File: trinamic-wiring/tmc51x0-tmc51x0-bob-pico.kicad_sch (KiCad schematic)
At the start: 4 parts, among them M1 Stepper_Motor

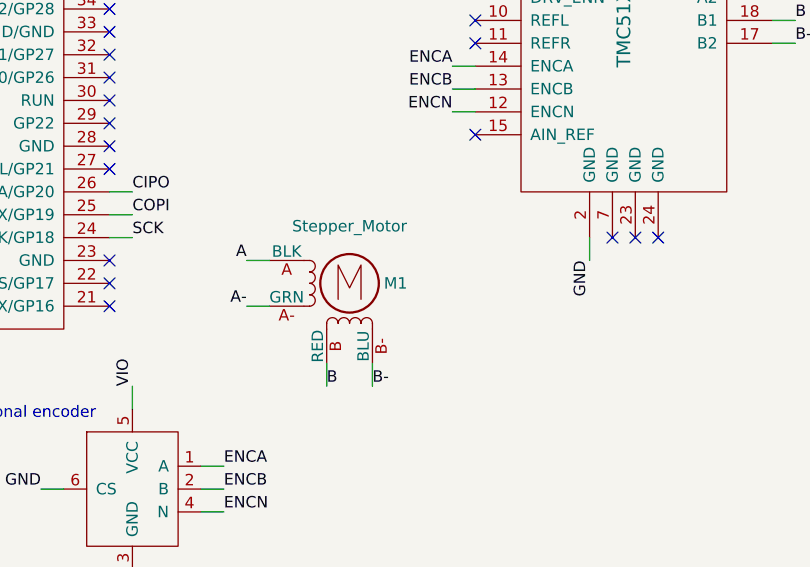
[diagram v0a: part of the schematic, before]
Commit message: Split tmc51x0 into spi and uart
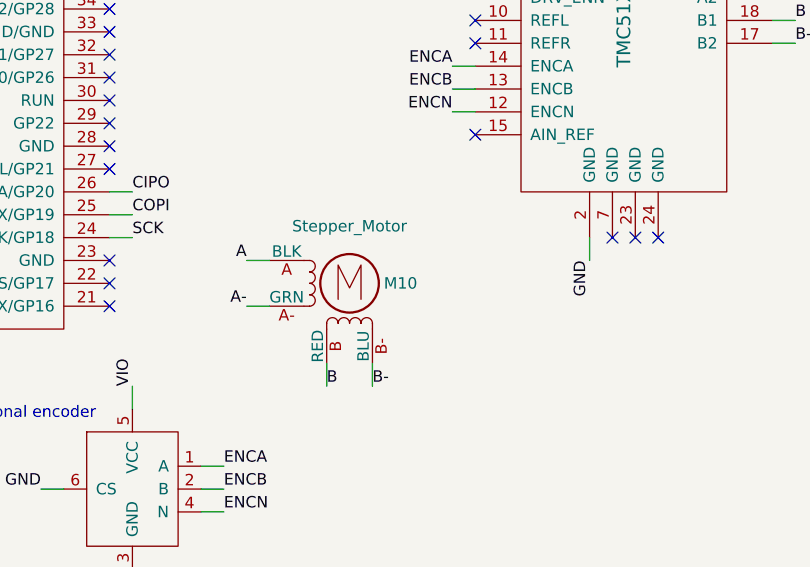
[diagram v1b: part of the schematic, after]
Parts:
- renumbered A3 to A5, BOB1 to BOB2, ENC1 to ENC2, M1 to M10
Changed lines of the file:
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@@
   (title_block
     (title "Trinamic Wiring")
-    (date "2024-07-31")
+    (date "2024-08-01")
     (rev "0.5")
     (company "Janelia Research Campus")
@@
   (symbol (lib_id "Janelia:Stepper_Motor_QSH2818-32-07-006") (at 149.86 133.35 0) (unit 1)
     (in_bom yes) (on_board yes) (dnp no)
-    (property "Reference" "M1" (at 153.67 133.35 0)
+    (property "Reference" "M10" (at 153.67 133.35 0)
       (effects (font (size 1.27 1.27)) (justify left))
     )
@@
     (instances
       (project "trinamic-wiring"
-        (path "/e4144788-6304-493f-818e-5d881d3b7418/a161638e-a96f-4455-865a-1d7502675f43/176cb0b5-cab1-47ac-9998-e59b71e39393/dab15df5-b51f-4c1f-8fc9-49b45f8778bf"
-          (reference "M1") (unit 1)
+        (path "/e4144788-6304-493f-818e-5d881d3b7418/a161638e-a96f-4455-865a-1d7502675f43/ca35872a-a0db-401c-97bd-5b4a3f731cf1/abe2ac4d-e9f3-44e3-a772-2451bb376256/dab15df5-b51f-4c1f-8fc9-49b45f8778bf"
+          (reference "M10") (unit 1)
         )
       )
@@
   (symbol (lib_id "Janelia:PICO_HEADERS") (at 80.01 111.76 0) (unit 1)
     (in_bom yes) (on_board yes) (dnp no) (fields_autoplaced)
-    (property "Reference" "A3" (at 115.57 82.55 0) (do_not_autoplace)
+    (property "Reference" "A5" (at 115.57 82.55 0) (do_not_autoplace)
       (effects (font (size 1.524 1.524)) hide)
     )
@@
     (instances
       (project "trinamic-wiring"
-        (path "/e4144788-6304-493f-818e-5d881d3b7418/a161638e-a96f-4455-865a-1d7502675f43/176cb0b5-cab1-47ac-9998-e59b71e39393/dab15df5-b51f-4c1f-8fc9-49b45f8778bf"
-          (reference "A3") (unit 1)
+        (path "/e4144788-6304-493f-818e-5d881d3b7418/a161638e-a96f-4455-865a-1d7502675f43/ca35872a-a0db-401c-97bd-5b4a3f731cf1/abe2ac4d-e9f3-44e3-a772-2451bb376256/dab15df5-b51f-4c1f-8fc9-49b45f8778bf"
+          (reference "A5") (unit 1)
         )
       )
@@
   (symbol (lib_id "Janelia:ENCODER_EMS22Q") (at 125.73 156.21 0) (unit 1)
     (in_bom yes) (on_board yes) (dnp no) (fields_autoplaced)
-    (property "Reference" "ENC1" (at 128.27 148.59 0)
+    (property "Reference" "ENC2" (at 128.27 148.59 0)
       (effects (font (size 1.524 1.524)) hide)
     )
@@
     (instances
       (project "trinamic-wiring"
-        (path "/e4144788-6304-493f-818e-5d881d3b7418/a161638e-a96f-4455-865a-1d7502675f43/176cb0b5-cab1-47ac-9998-e59b71e39393/dab15df5-b51f-4c1f-8fc9-49b45f8778bf"
-          (reference "ENC1") (unit 1)
+        (path "/e4144788-6304-493f-818e-5d881d3b7418/a161638e-a96f-4455-865a-1d7502675f43/ca35872a-a0db-401c-97bd-5b4a3f731cf1/abe2ac4d-e9f3-44e3-a772-2451bb376256/dab15df5-b51f-4c1f-8fc9-49b45f8778bf"
+          (reference "ENC2") (unit 1)
         )
       )
@@
   (symbol (lib_id "Janelia:TMC51X0_BOB") (at 180.34 102.87 0) (unit 1)
     (in_bom yes) (on_board yes) (dnp no)
-    (property "Reference" "BOB1" (at 180.34 129.54 0)
+    (property "Reference" "BOB2" (at 180.34 129.54 0)
       (effects (font (size 1.524 1.524)) hide)
     )
@@
     (instances
       (project "trinamic-wiring"
-        (path "/e4144788-6304-493f-818e-5d881d3b7418/a161638e-a96f-4455-865a-1d7502675f43/176cb0b5-cab1-47ac-9998-e59b71e39393/dab15df5-b51f-4c1f-8fc9-49b45f8778bf"
-          (reference "BOB1") (unit 1)
+        (path "/e4144788-6304-493f-818e-5d881d3b7418/a161638e-a96f-4455-865a-1d7502675f43/ca35872a-a0db-401c-97bd-5b4a3f731cf1/abe2ac4d-e9f3-44e3-a772-2451bb376256/dab15df5-b51f-4c1f-8fc9-49b45f8778bf"
+          (reference "BOB2") (unit 1)
         )
       )
